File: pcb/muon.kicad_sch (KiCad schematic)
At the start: 55 parts, among them J1 Debug Pins, J2 USB_C_Receptacle_USB2.0, SW1 Kailh Hotswap, SW2 Kailh Hotswap, SW3 Reset, SW4 DTSM-66R-V-T/R, SW5 DTSM-66R-V-T/R, SW6 DTSM-66R-V-T/R, SW7 Kailh Hotswap, U1 SRV05-4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

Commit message: revised v0.4, hybrid hotswap socket, fix off-center switches (off by .5mm)
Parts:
- SW1, SW2, SW7: footprint Keyswitch:SW_Hotswap_Kailh_MX_1.00u -> local-hybrid:SW_Hotswap_Hybrid_1.00u
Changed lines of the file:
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@@
     (property "Reference" "SW7" (id 0) (at 205.74 85.09 0))
     (property "Value" "Kailh Hotswap" (id 1) (at 220.98 73.66 0))
-    (property "Footprint" "Keyswitch:SW_Hotswap_Kailh_MX_1.00u" (id 2) (at 210.82 82.55 0)
+    (property "Footprint" "local-hybrid:SW_Hotswap_Hybrid_1.00u" (id 2) (at 210.82 82.55 0)
       (effects (font (size 1.27 1.27)) hide)
     )
@@
     (property "Reference" "SW2" (id 0) (at 205.74 81.28 0))
     (property "Value" "Kailh Hotswap" (id 1) (at 220.98 73.66 0))
-    (property "Footprint" "Keyswitch:SW_Hotswap_Kailh_MX_1.00u" (id 2) (at 210.82 78.74 0)
+    (property "Footprint" "local-hybrid:SW_Hotswap_Hybrid_1.00u" (id 2) (at 210.82 78.74 0)
       (effects (font (size 1.27 1.27)) hide)
     )
@@
     (property "Reference" "SW1" (id 0) (at 205.74 77.47 0))
     (property "Value" "Kailh Hotswap" (id 1) (at 220.98 73.66 0))
-    (property "Footprint" "Keyswitch:SW_Hotswap_Kailh_MX_1.00u" (id 2) (at 210.82 74.93 0)
+    (property "Footprint" "local-hybrid:SW_Hotswap_Hybrid_1.00u" (id 2) (at 210.82 74.93 0)
       (effects (font (size 1.27 1.27)) hide)
     )
@@
     )
     (path "/e28f19a7-3a6b-4f2f-a696-440e65890057"
-      (reference "SW1") (unit 1) (value "Kailh Hotswap") (footprint "Keyswitch:SW_Hotswap_Kailh_MX_1.00u")
+      (reference "SW1") (unit 1) (value "Kailh Hotswap") (footprint "local-hybrid:SW_Hotswap_Hybrid_1.00u")
     )
     (path "/b16ffb25-b666-4ad7-810c-9718043c8c31"
-      (reference "SW2") (unit 1) (value "Kailh Hotswap") (footprint "Keyswitch:SW_Hotswap_Kailh_MX_1.00u")
+      (reference "SW2") (unit 1) (value "Kailh Hotswap") (footprint "local-hybrid:SW_Hotswap_Hybrid_1.00u")
     )
     (path "/345bff2e-14b2-4e71-b596-e413e96ff762"
@@
     )
     (path "/881fa7cb-bfeb-4b04-92ad-9614e3d4e1df"
-      (reference "SW7") (unit 1) (value "Kailh Hotswap") (footprint "Keyswitch:SW_Hotswap_Kailh_MX_1.00u")
+      (reference "SW7") (unit 1) (value "Kailh Hotswap") (footprint "local-hybrid:SW_Hotswap_Hybrid_1.00u")
     )
     (path "/0a75f060-9ad0-4ebe-ae07-34bbdb9c610f"

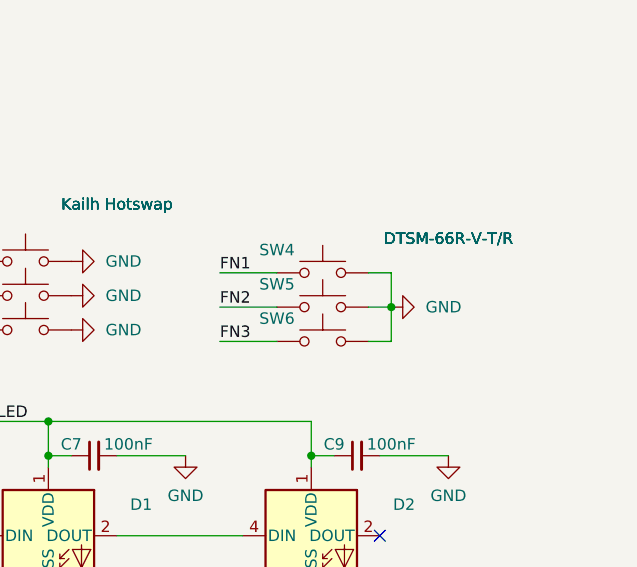
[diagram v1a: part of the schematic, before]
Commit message: Change buttons and move them into place Update 3D models
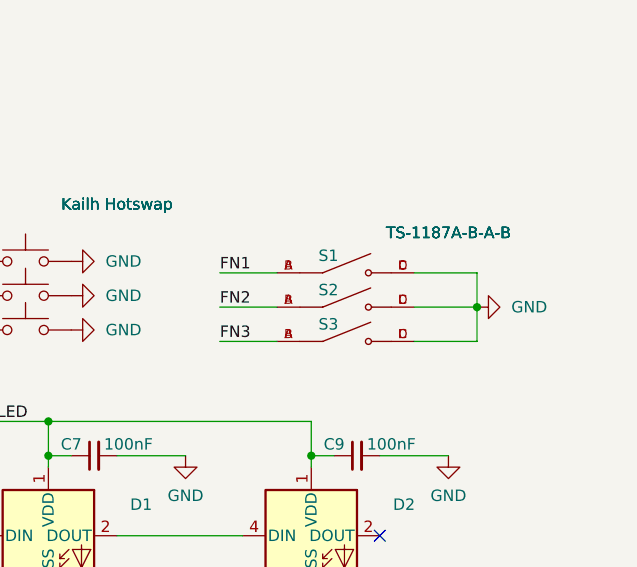
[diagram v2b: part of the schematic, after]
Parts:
- removed SW4, SW5, SW6: DTSM-66R-V-T/R, Button_Switch_SMD:SW_Push_1P1T_NO_6x6mm_H9.5mm, symbol Switch:SW_Push
- added S1, S2, S3: TS-1187A-B-A-B, SW_TS-1187A-B-A-B, symbol button:TS-1187A-B-A-B
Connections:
- net FN1: now also S1.A, S1.B
- net FN2: now also S2.A, S2.B
- net FN3: now also S3.A, S3.B
- net GND: now also S1.C, S1.D, S2.C, S2.D, S3.C, S3.D

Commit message: broad strokes
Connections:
- net D+: now also U1.3 (IO2); no longer U1.4 (IO3)
- net D-: now also U1.4 (IO3); no longer U1.3 (IO2)
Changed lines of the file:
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@@
     (effects (font (size 1.27 1.27)) (justify right bottom))
   )
-  (label "D+" (at 44.45 88.9 180)
+  (label "D+" (at 44.45 83.82 180)
     (effects (font (size 1.27 1.27)) (justify right bottom))
   )
@@
     (effects (font (size 1.27 1.27)) (justify left bottom))
   )
-  (label "D-" (at 44.45 83.82 180)
+  (label "D-" (at 44.45 88.9 180)
     (effects (font (size 1.27 1.27)) (justify right bottom))
   )

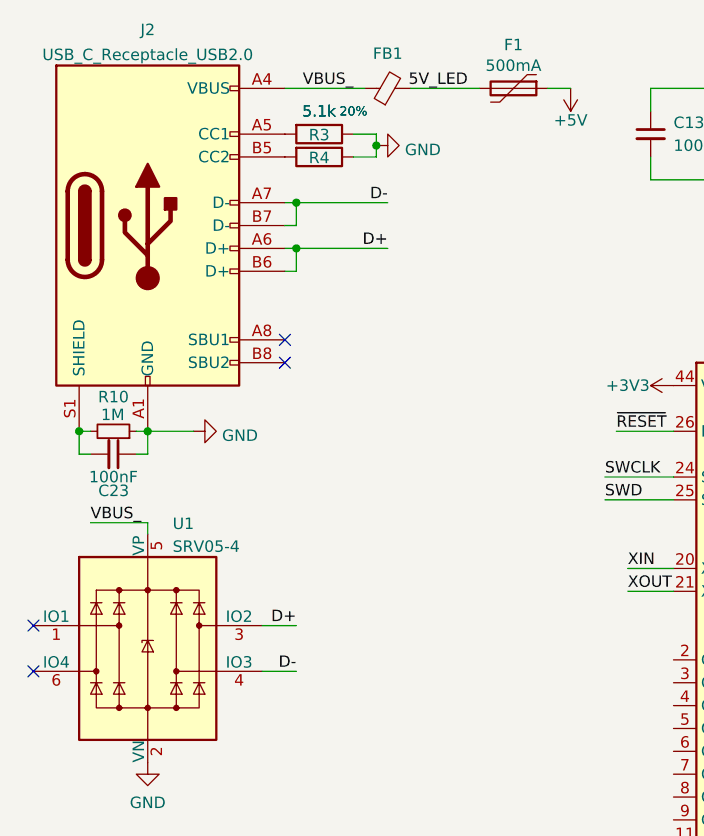
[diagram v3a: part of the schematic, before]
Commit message: usb back on main side
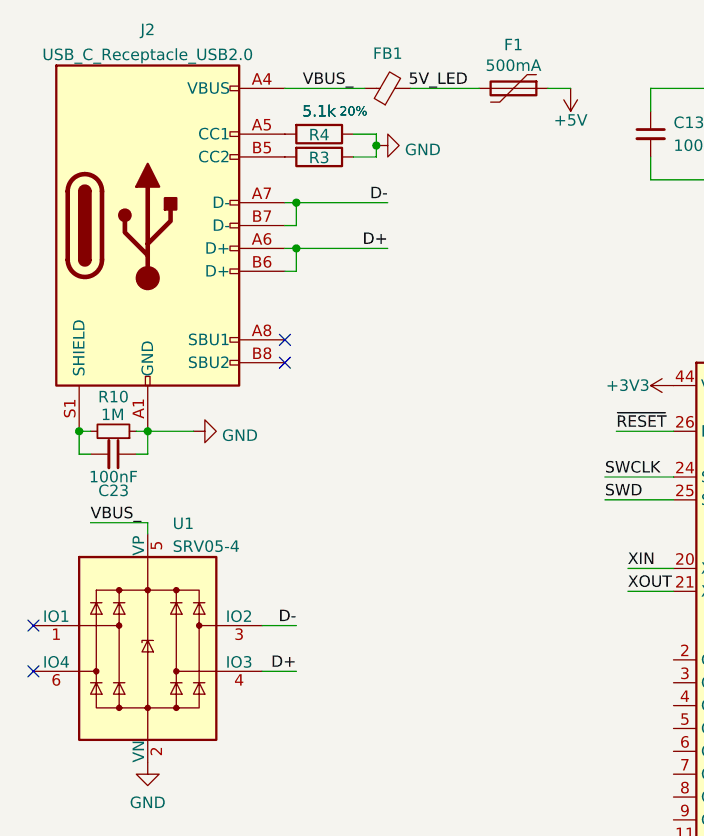
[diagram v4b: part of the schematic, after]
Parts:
- renumbered R4 to R3, R3 to R4
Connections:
- net D+: now also U1.4 (IO3); no longer U1.3 (IO2)
- net D-: now also U1.3 (IO2); no longer U1.4 (IO3)
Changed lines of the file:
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@@
     (effects (font (size 1.27 1.27)) (justify right bottom))
   )
-  (label "D+" (at 44.45 83.82 180)
+  (label "D-" (at 44.45 83.82 180)
     (effects (font (size 1.27 1.27)) (justify right bottom))
   )
@@
     (effects (font (size 1.27 1.27)) (justify left bottom))
   )
-  (label "D-" (at 44.45 88.9 180)
+  (label "D+" (at 44.45 88.9 180)
     (effects (font (size 1.27 1.27)) (justify right bottom))
   )
@@
   (symbol (lib_id "Device:R") (at 46.99 29.21 270) (unit 1)
     (in_bom yes) (on_board yes)
-    (property "Reference" "R3" (id 0) (at 46.99 29.3074 90))
+    (property "Reference" "R4" (id 0) (at 46.99 29.3074 90))
     (property "Value" "5.1k" (id 1) (at 46.99 26.67 90))
     (property "Footprint" "Resistor_SMD:R_0402_1005Metric" (id 2) (at 46.99 27.432 90)
@@
   (symbol (lib_id "Device:R") (at 46.99 31.75 270) (unit 1)
     (in_bom yes) (on_board yes)
-    (property "Reference" "R4" (id 0) (at 46.99 31.8474 90))
+    (property "Reference" "R3" (id 0) (at 46.99 31.8474 90))
     (property "Value" "5.1k" (id 1) (at 46.99 26.67 90))
     (property "Footprint" "Resistor_SMD:R_0402_1005Metric" (id 2) (at 46.99 29.972 90)
@@
       (reference "R2") (unit 1) (value "220") (footprint "Resistor_SMD:R_0402_1005Metric")
     )
+    (path "/fb6df40b-a201-4cf2-bb16-75569bcefcca"
+      (reference "R3") (unit 1) (value "5.1k") (footprint "Resistor_SMD:R_0402_1005Metric")
+    )
     (path "/3a8cb071-4bda-4fc9-8c8b-585e54604573"
-      (reference "R3") (unit 1) (value "5.1k") (footprint "Resistor_SMD:R_0402_1005Metric")
-    )
-    (path "/fb6df40b-a201-4cf2-bb16-75569bcefcca"
       (reference "R4") (unit 1) (value "5.1k") (footprint "Resistor_SMD:R_0402_1005Metric")
     )

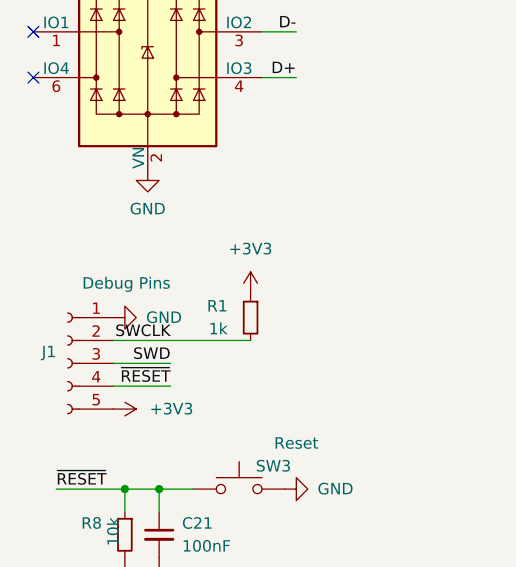
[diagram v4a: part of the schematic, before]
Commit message: Pre-v0.6 - use TagConnect debug header - equally space underglow LEDs - add comment to replicate kibuzzard settings - use M3 mounting holes
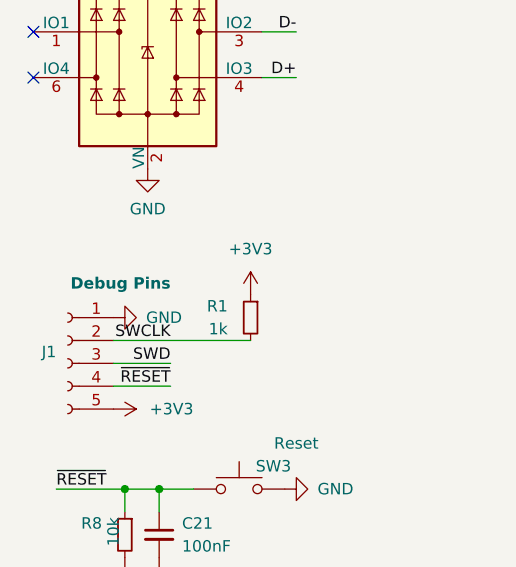
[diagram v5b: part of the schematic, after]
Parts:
- J1: footprint Connector_PinHeader_2.00mm:PinHeader_1x05_P2.00mm_Vertical -> Connector:Tag-Connect_TC2030-IDC-NL_2x03_P1.27mm_Vertical
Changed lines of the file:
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@@
     )
     (property "Value" "Debug Pins" (id 1) (at 30.48 111.76 0)
-      (effects (font (size 1.27 1.27)) (justify left))
-    )
-    (property "Footprint" "Connector_PinHeader_2.00mm:PinHeader_1x05_P2.00mm_Vertical" (id 2) (at 19.05 120.65 0)
+      (effects (font (size 1.27 1.27) bold) (justify left))
+    )
+    (property "Footprint" "Connector:Tag-Connect_TC2030-IDC-NL_2x03_P1.27mm_Vertical" (id 2) (at 19.05 120.65 0)
       (effects (font (size 1.27 1.27)) hide)
     )
@@
     )
     (path "/0ff39221-c92f-4e4d-a18b-e53c9e597d78"
-      (reference "J1") (unit 1) (value "Debug Pins") (footprint "Connector_PinHeader_2.00mm:PinHeader_1x05_P2.00mm_Vertical")
+      (reference "J1") (unit 1) (value "Debug Pins") (footprint "Connector:Tag-Connect_TC2030-IDC-NL_2x03_P1.27mm_Vertical")
     )
     (path "/181a118b-aef0-401e-b0d6-eeb72ac7cbc9"
